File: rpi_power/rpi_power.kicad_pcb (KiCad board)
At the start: 2 copper layers, 69 x 57.4 mm, 67 parts, among them J1 POWER, J2 Raspberry_Pi_2_3, J3 Raspberry_Pi_2_3, J4 ADCs, J7 PROG, J9 GPIO, Q10 IRLML6344TRPBF, Q6 IRLML6344TRPBF, U1 TPS54625, U2 ATxmega16A4U-AU, U3 LM2936-3.3, Y1 Crystal

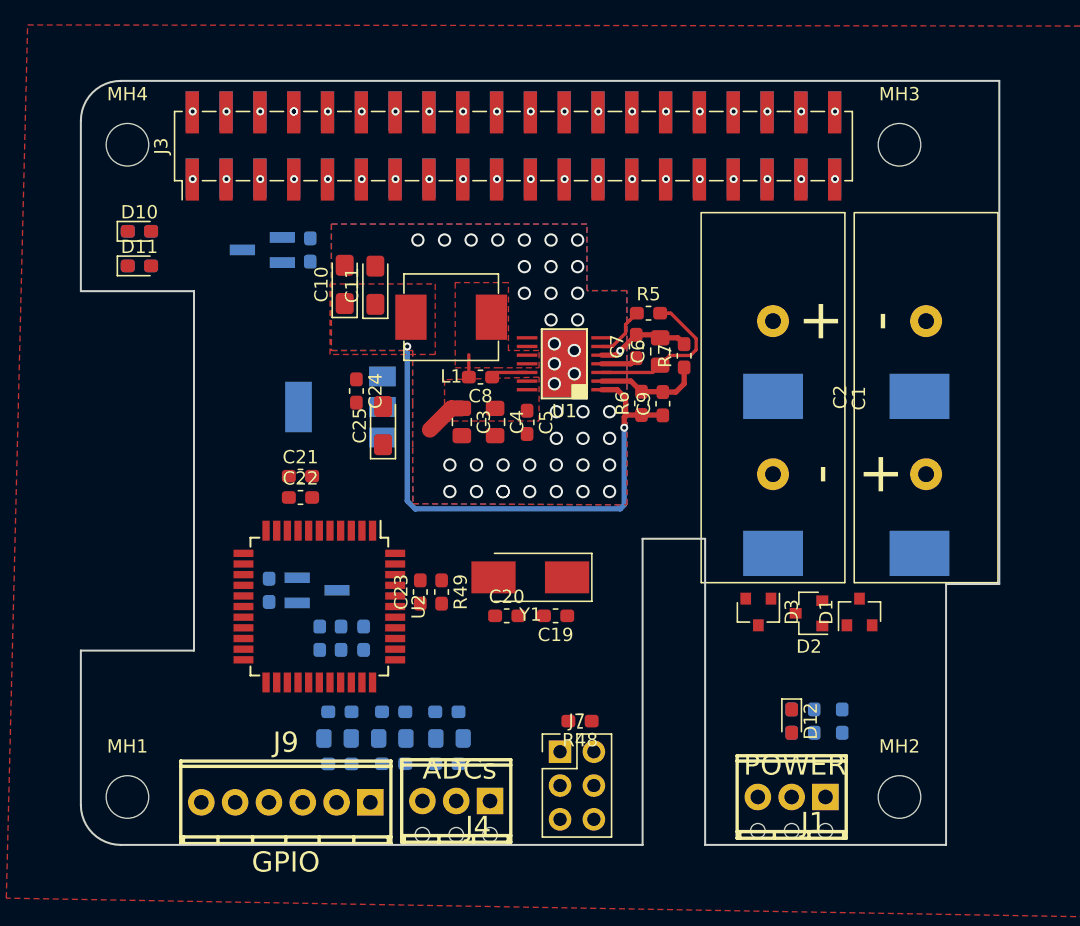
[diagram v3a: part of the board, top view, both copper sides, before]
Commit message: Updated some footprints.
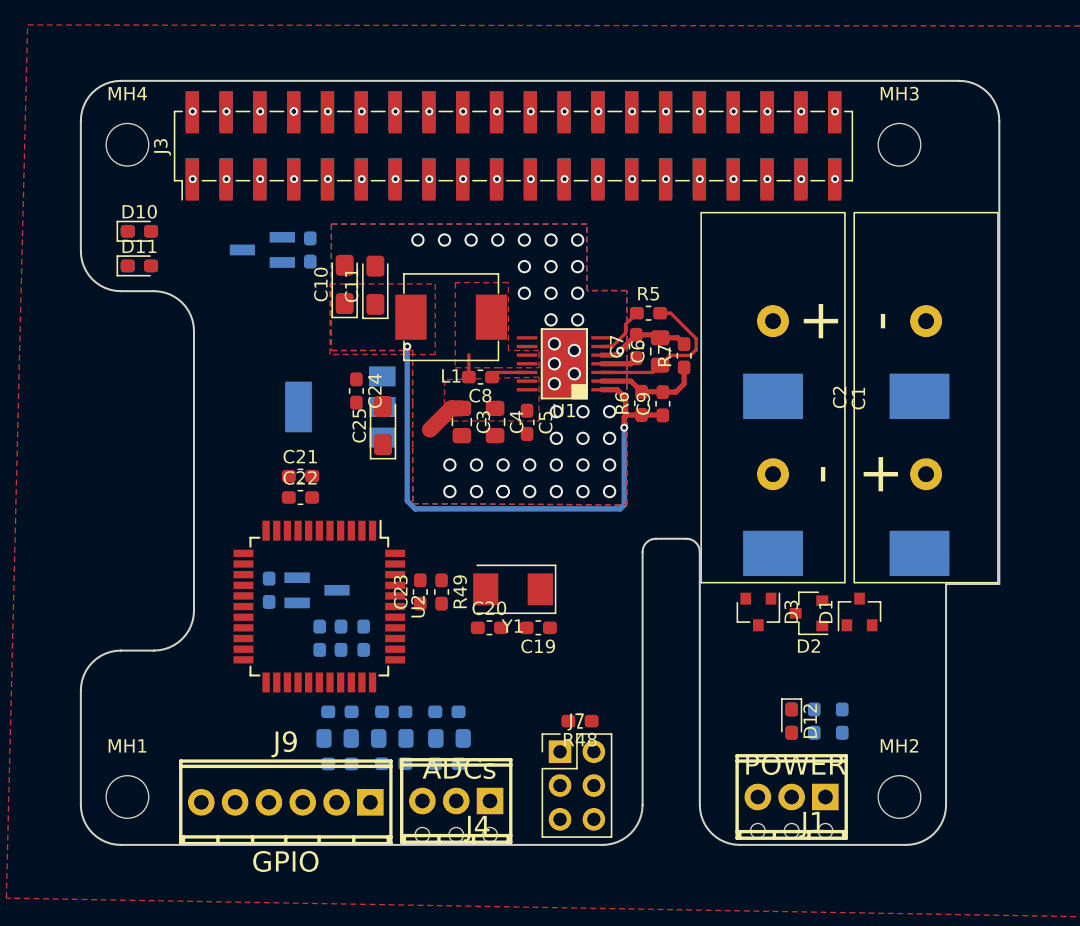
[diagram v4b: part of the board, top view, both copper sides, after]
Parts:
- C10, C11, C25: footprint Capacitor_Tantalum_SMD:CP_EIA-3216-10_Kemet-I_Pad1.58x1.35mm_HandSolder -> Capacitors:Tantalum_SMD_3216_KEMET_T491_HandSolder
- Y1: footprint Crystal:Crystal_SMD_Abracon_ABM3-2Pin_5.0x3.2mm_HandSoldering -> Crystals:Crystal_SMD_Abracon_ABM3-2Pin_5.0x3.2mm
- moved C19 1.58 mm to (150.9, 107.3)
- moved Y1 1.58 mm to (149.0, 104.4)
- moved C20 1.58 mm to (147.2, 107.3)
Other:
- outline, holes or cut-outs redrawn

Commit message: Routing done, pending review.
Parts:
- C12, C13, C14: footprint Capacitor_SMD:C_0805_2012Metric_Pad1.15x1.40mm_HandSolder -> Capacitor_SMD:C_0603_1608Metric_Pad1.05x0.95mm_HandSolder
- C21, C22, C23: moved to B.Cu
- U1: footprint TexasInstruments:HTSSOP-14-PWP -> TexasInstruments:HTSSOP-14-PWP_Handsolder
- moved R32 18.8 mm to (152.3, 102.2), turned to 180 degrees
- moved R31 16.4 mm to (152.3, 100.6), turned to 0 degrees
- moved R30 13.8 mm to (144.3, 102.2)
- moved Q6 13.7 mm to (147.8, 102.2)
- moved C14 8.87 mm to (138.5, 108.8), turned to 90 degrees
- moved C13 7.43 mm to (136.9, 108.8), turned to 90 degrees
- moved C12 6.82 mm to (135.3, 108.8), turned to 90 degrees
- moved C21 6.70 mm to (132.8, 102.6), turned to 270 degrees
- moved C19 6.12 mm to (144.8, 108.2), turned to 270 degrees
- moved R12 5.44 mm to (148.6, 114.6), turned to 90 degrees
- moved C22 5.41 mm to (131.2, 102.6), turned to 270 degrees
- moved D12 4.70 mm to (169.9, 109.6)
- moved R1 4.70 mm to (169.9, 109.6)
- moved R2 4.70 mm to (171.6, 109.6)
- moved R47 4.70 mm to (173.7, 109.6)
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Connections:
- J2 pad 1: +3V3 -> 1
- J2 pad 17: +3V3 -> 17
- J3 pad 1: +3V3 -> 1
- J3 pad 17: +3V3 -> 17
- J7 pad 3: (no net) -> Net-(J7-Pad3)
- J7 pad 4: (no net) -> Net-(J7-Pad4)
- U2 pad 1: (no net) -> Net-(U2-Pad1)
- U2 pad 12: (no net) -> Net-(U2-Pad12)
- U2 pad 13: (no net) -> Net-(U2-Pad13)
- U2 pad 14: (no net) -> Net-(U2-Pad14)
- U2 pad 15: (no net) -> Net-(U2-Pad15)
- U2 pad 16: (no net) -> Net-(U2-Pad16)
- U2 pad 17: (no net) -> Net-(U2-Pad17)
- U2 pad 2: (no net) -> Net-(U2-Pad2)
- U2 pad 20: (no net) -> Net-(U2-Pad20)
- U2 pad 21: (no net) -> Net-(U2-Pad21)
- U2 pad 22: (no net) -> Net-(U2-Pad22)
- U2 pad 3: (no net) -> Net-(U2-Pad3)
- U2 pad 40: (no net) -> Net-(U2-Pad40)
- U2 pad 41: (no net) -> Net-(U2-Pad41)
- U2 pad 42: (no net) -> Net-(U2-Pad42)
- U2 pad 43: (no net) -> Net-(U2-Pad43)
- U2 pad 44: (no net) -> Net-(U2-Pad44)
- U2 pad 5: WATCHDOG -> ENABLE
- U2 pad 7: ENABLE -> WATCHDOG
- U3 pad 4: (no net) -> GND
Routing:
- net POWER_STATE: track 0.00 -> 87.7 mm, vias 1 -> 2
- net VCC: track 0.00 -> 66.4 mm, vias 0 -> 5
- net VCOND: track 3.06 -> 67.6 mm, vias 0 -> 2
- net ENABLE: track 0.00 -> 53.3 mm, vias 0 -> 2
- net LED_RUN: track 0.00 -> 42.3 mm
- net +5V: track 41.2 -> 82.8 mm, vias 4 -> 3
- net WATCHDOG: track 0.00 -> 34.3 mm, vias 1 -> 3
- net I2C_SDA: track 0.00 -> 28.0 mm, vias 1 -> 3
- net +12V: track 0.00 -> 27.7 mm, vias 0 -> 1
- net ADC0: track 0.00 -> 27.7 mm, vias 0 -> 1
- net I2C_SCL: track 0.00 -> 26.6 mm, vias 1 -> 3
- net PDI_CLK: track 0.00 -> 23.3 mm
- net Net-(C1-Pad1): track 0.00 -> 22.2 mm, vias 0 -> 1
- net Net-(C15-Pad2): track 0.00 -> 21.3 mm
- net Net-(D1-Pad1): track 0.00 -> 19.1 mm, vias 0 -> 1
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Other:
- outline, holes or cut-outs redrawn
- board text added: "+12V"
- board text added: "+5V ON"
- board text added: "ADC1"
- board text added: "ADC2"
- board text added: "ADC3"
- board text added: "GND"
- board text added: "GPIO0"
- board text added: "GPIO1"
- board text added: "GPIO2"
- board text added: "GPIO3"
- board text added: "GPIO4"
- board text added: "RUN"
- board text added: "VCOND"

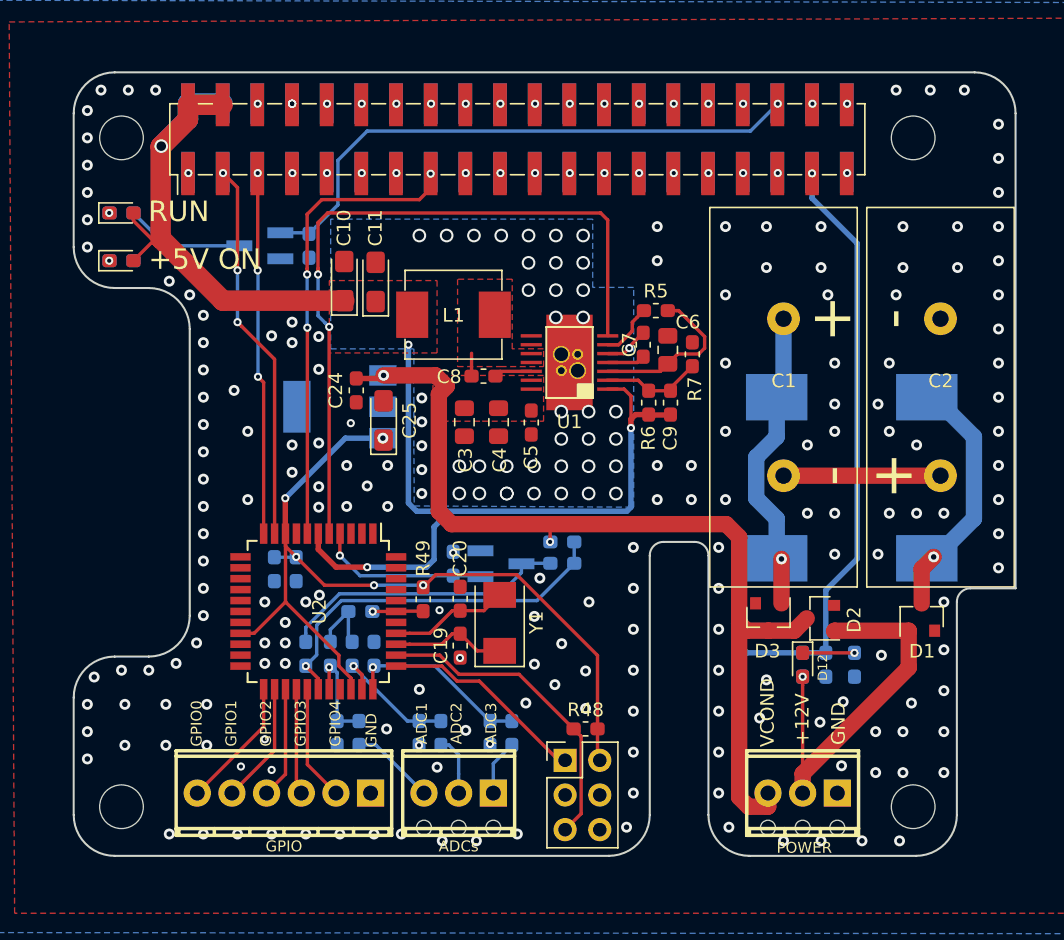
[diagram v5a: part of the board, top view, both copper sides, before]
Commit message: Routing and silkscreen done.
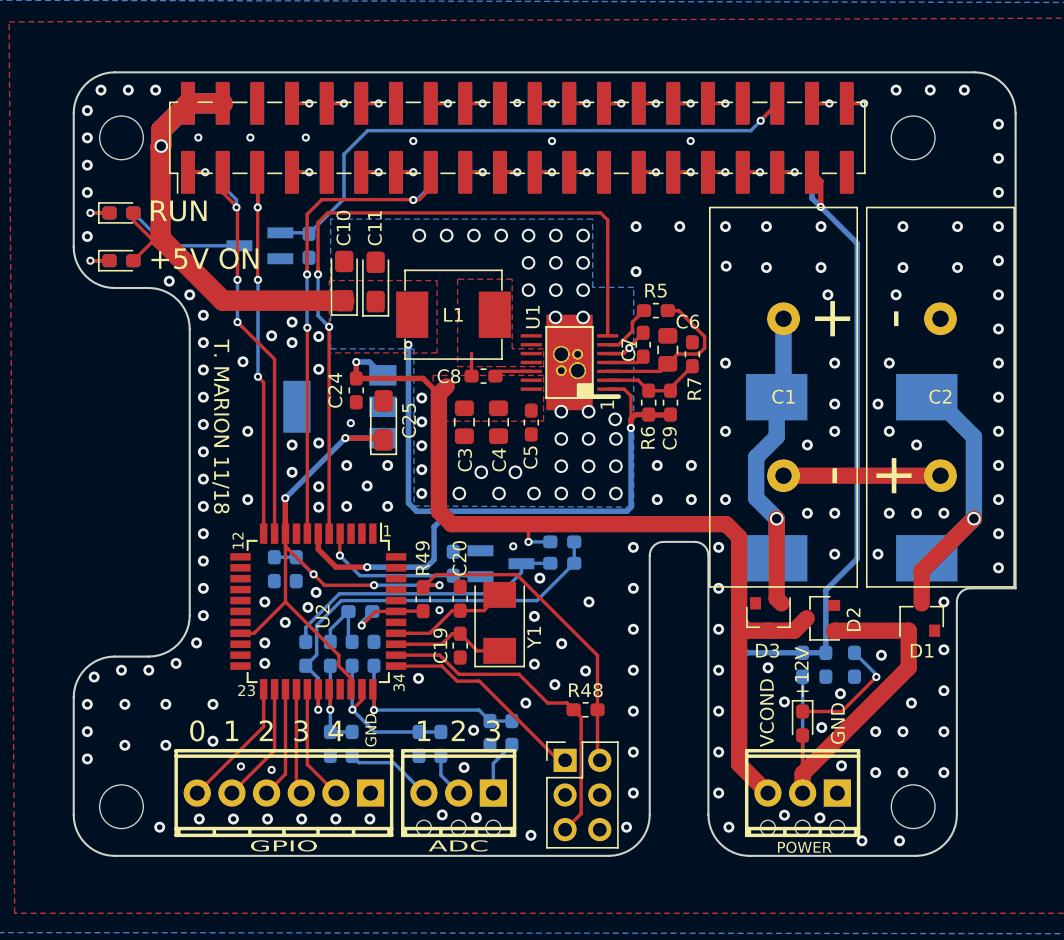
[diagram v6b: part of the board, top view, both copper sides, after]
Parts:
- added G***: LOGO, Logos:taz, B.Cu at (160.4, 84.1)
- J4: value ADCs -> ADC
- moved D12 4.30 mm to (169.9, 113.9)
- moved R48 1.40 mm to (154.0, 112.9)
- moved R8 0.94 mm to (136.9, 115.4)
- moved R9 0.94 mm to (135.3, 115.4)
- moved R10 0.80 mm to (143.4, 115.4)
- moved R11 0.80 mm to (141.8, 115.4)
- moved J3 0.10 mm to (149.0, 71.0)
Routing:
- net VCC: track 66.4 -> 73.5 mm
- net Net-(D12-Pad1): track 3.80 -> 8.88 mm
- net +12V: track 27.7 -> 31.9 mm, vias 1 -> 0
- net Net-(D1-Pad1): track 19.1 -> 23.1 mm
- net Net-(C1-Pad1): track 22.2 -> 25.3 mm
- net ADC0: track 27.7 -> 30.7 mm
- net I2C_SDA: track 28.0 -> 31.0 mm
- net POWER_STATE: track 87.7 -> 90.5 mm
- net Net-(D11-Pad1): track 0.00 -> 2.80 mm
- net Net-(D10-Pad1): track 0.00 -> 2.80 mm
- net VCOND: track 67.6 -> 70.3 mm
- net WATCHDOG: track 34.3 -> 37.0 mm
- net I2C_SCL: track 26.6 -> 29.2 mm
- net Net-(C23-Pad1): track 3.71 -> 6.28 mm
- net 40: track 0.00 -> 2.54 mm
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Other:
- board text added: "0"
- board text added: "1"
- board text added: "12"
- board text added: "2"
- board text added: "23"
- board text added: "3"
- board text added: "34"
- board text added: "4"
- board text added: "RPi_power Rev. A"
- board text added: "T. MARION 11/18"
- board text added: "https://github.com/Talw3g/rpi_power_board"
- board text removed: "ADC1"
- board text removed: "ADC2"
- board text removed: "ADC3"
- board text removed: "GPIO0"
- board text removed: "GPIO1"
- board text removed: "GPIO2"
- board text removed: "GPIO3"
- board text removed: "GPIO4"

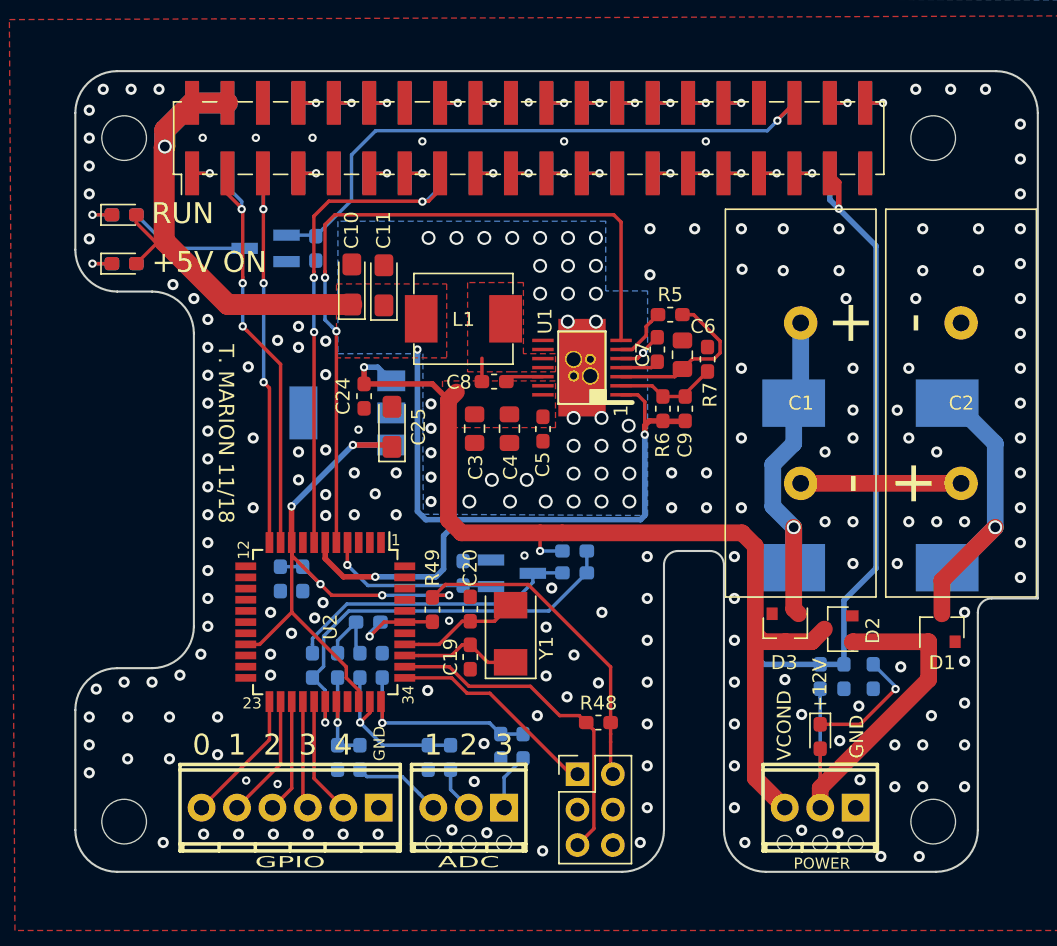
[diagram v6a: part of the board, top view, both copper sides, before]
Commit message: Differentiated VCOND and BATT+. Routing done.
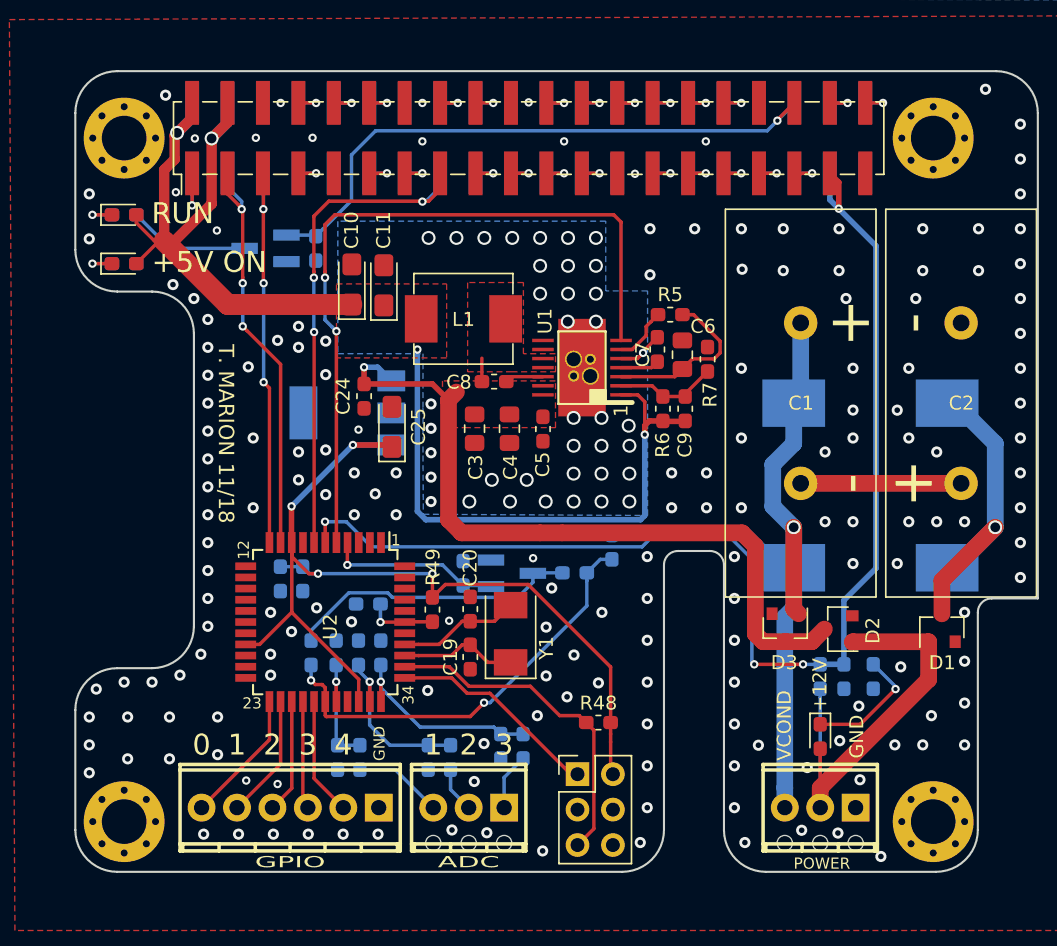
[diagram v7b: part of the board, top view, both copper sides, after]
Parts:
- MH1, MH2, MH3, MH4: footprint MountingHole:MountingHole_3.2mm_M3_DIN965 -> Pads:MountingHole_M3-5.8_Pad_Via
- moved R31 2.69 mm to (155.0, 100.3), turned to 270 degrees
- moved C23 1.30 mm to (137.5, 104.4)
- moved C12 0.91 mm to (135.2, 107.9)
- moved C13 0.91 mm to (136.8, 107.9)
- moved C14 0.91 mm to (138.4, 107.9)
- moved C15 0.91 mm to (133.4, 107.9)
- moved G*** 0.21 mm to (160.2, 84.2)
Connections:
- net VCOND_MEASURE renamed BATT+_MEASURE
- C1 pad 1: Net-(C1-Pad1) -> BATT+
- D3 pad 2: Net-(C1-Pad1) -> BATT+
- J1 pad 3: VCOND -> BATT+
- J7 pad 3: Net-(J7-Pad3) -> (no net)
- J7 pad 4: Net-(J7-Pad4) -> (no net)
- R3 pad 1: Net-(C1-Pad1) -> BATT+
- R31 pad 1: VCOND -> BATT+
- R4 pad 1: Net-(C1-Pad1) -> BATT+
- U2 pad 1: Net-(U2-Pad1) -> (no net)
- U2 pad 12: Net-(U2-Pad12) -> (no net)
- U2 pad 13: Net-(U2-Pad13) -> (no net)
- U2 pad 14: Net-(U2-Pad14) -> (no net)
- U2 pad 15: Net-(U2-Pad15) -> (no net)
- U2 pad 16: Net-(U2-Pad16) -> (no net)
- U2 pad 17: Net-(U2-Pad17) -> (no net)
- U2 pad 2: Net-(U2-Pad2) -> (no net)
- U2 pad 20: Net-(U2-Pad20) -> (no net)
- U2 pad 21: Net-(U2-Pad21) -> (no net)
- U2 pad 22: Net-(U2-Pad22) -> (no net)
- U2 pad 3: Net-(U2-Pad3) -> (no net)
- U2 pad 40: Net-(U2-Pad40) -> (no net)
- U2 pad 41: Net-(U2-Pad41) -> (no net)
- U2 pad 42: Net-(U2-Pad42) -> (no net)
- U2 pad 43: Net-(U2-Pad43) -> (no net)
- U2 pad 44: Net-(U2-Pad44) -> (no net)
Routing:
- net BATT+: track 0.00 -> 57.0 mm, vias 0 -> 1
- net Net-(C1-Pad1): track 25.3 -> 0.00 mm, vias 1 -> 0
- net VCOND: track 70.3 -> 54.1 mm, vias 2 -> 1
- net +5V: track 82.9 -> 91.7 mm, vias 3 -> 4
- net GND: track 10.9 -> 6.22 mm, vias 222 -> 214
- net POWER_STATE: track 90.5 -> 88.2 mm, vias 2 -> 4
- net 1: track 2.54 -> 4.61 mm
- net VCC: track 73.5 -> 71.6 mm, vias 5 -> 4
- net Net-(C23-Pad1): track 6.28 -> 5.04 mm
- net ADC1: track 7.98 -> 8.82 mm
- net ADC3: track 15.2 -> 14.6 mm
- net ADC0: track 30.7 -> 31.0 mm, vias 1 -> 2
